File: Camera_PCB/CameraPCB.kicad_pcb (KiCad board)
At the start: 6 copper layers, 51 parts, among them J2 USB_A, U1 V3s-eLQFP128, Y2 Crystal_GND3, Y4 Crystal_GND24

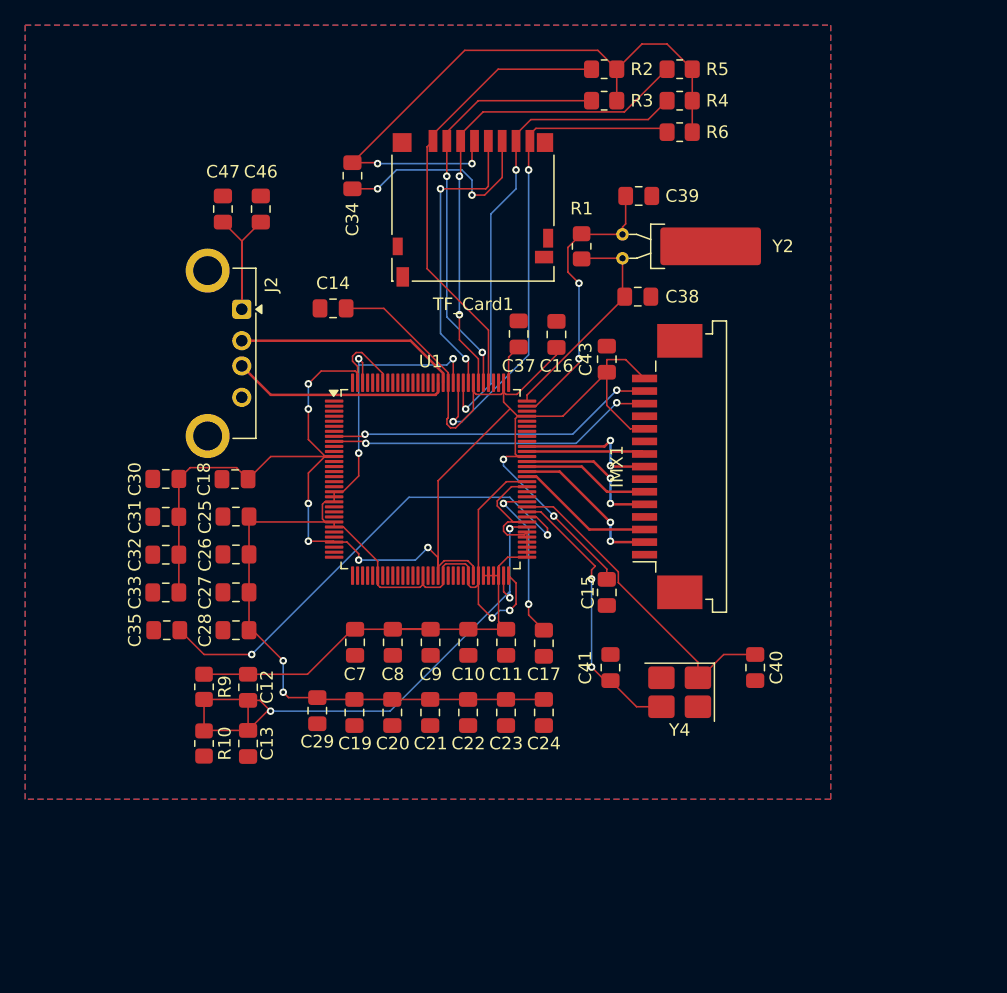
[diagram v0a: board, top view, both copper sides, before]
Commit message: Schematic done, thoroughly reviewed by Jack, should get reviewed by Connor if possible.
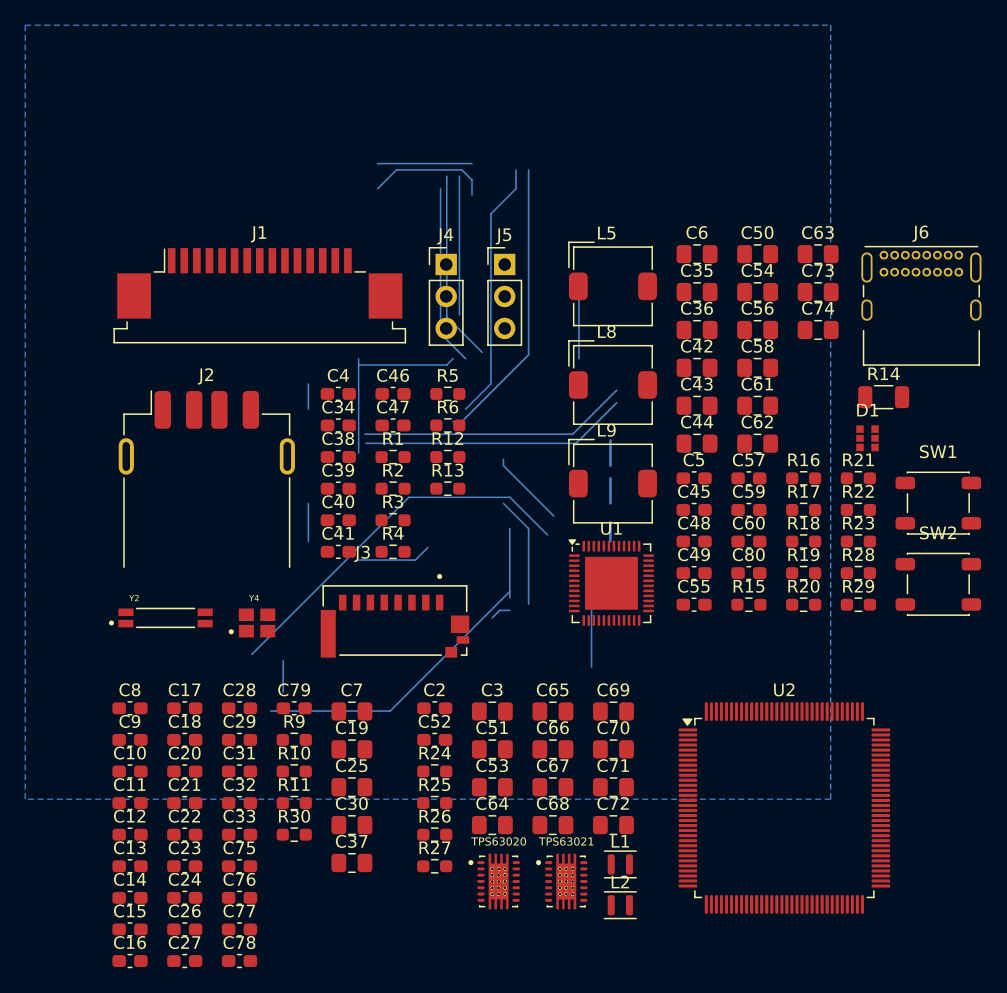
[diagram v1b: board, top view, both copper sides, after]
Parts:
- removed IMX1: ~, Connector_FFC-FPC:TE_1-84952-5_1x15-1MP_P1.0mm_Horizontal
- removed TF_Card1: ~, Connector_Card:microSD_HC_Hirose_DM3D-SF
- added C2: 0.1u, Capacitor_SMD:C_0603_1608Metric_Pad1.08x0.95mm_HandSolder, F.Cu at (148.0, 125.3)
- added C3: 22u, Capacitor_SMD:C_0805_2012Metric_Pad1.18x1.45mm_HandSolder, F.Cu at (152.6, 125.5)
- added C36: 10u, Capacitor_SMD:C_0805_2012Metric_Pad1.18x1.45mm_HandSolder, F.Cu at (168.9, 95.2)
- added C4: 1u, Capacitor_SMD:C_0603_1608Metric_Pad1.08x0.95mm_HandSolder, F.Cu at (140.4, 100.3)
- added C42: 10u, Capacitor_SMD:C_0805_2012Metric_Pad1.18x1.45mm_HandSolder, F.Cu at (168.9, 98.2)
- added C44: 4.7u, Capacitor_SMD:C_0805_2012Metric_Pad1.18x1.45mm_HandSolder, F.Cu at (168.9, 104.2)
- added C45: 0.1u, Capacitor_SMD:C_0603_1608Metric_Pad1.08x0.95mm_HandSolder, F.Cu at (168.7, 109.5)
- added C48: 1u, Capacitor_SMD:C_0603_1608Metric_Pad1.08x0.95mm_HandSolder, F.Cu at (168.7, 112.0)
- added C49: 1u, Capacitor_SMD:C_0603_1608Metric_Pad1.08x0.95mm_HandSolder, F.Cu at (168.7, 114.5)
- added C5: 1u, Capacitor_SMD:C_0603_1608Metric_Pad1.08x0.95mm_HandSolder, F.Cu at (168.7, 107.0)
- added C50: 10u, Capacitor_SMD:C_0805_2012Metric_Pad1.18x1.45mm_HandSolder, F.Cu at (173.7, 89.2)
- added C51: 22u, Capacitor_SMD:C_0805_2012Metric_Pad1.18x1.45mm_HandSolder, F.Cu at (152.6, 128.5)
- added C52: 0.1u, Capacitor_SMD:C_0603_1608Metric_Pad1.08x0.95mm_HandSolder, F.Cu at (148.0, 127.8)
- added C53: 10u, Capacitor_SMD:C_0805_2012Metric_Pad1.18x1.45mm_HandSolder, F.Cu at (152.6, 131.5)
- added C54: 10u, Capacitor_SMD:C_0805_2012Metric_Pad1.18x1.45mm_HandSolder, F.Cu at (173.7, 92.2)
- added C55: 1n, Capacitor_SMD:C_0603_1608Metric_Pad1.08x0.95mm_HandSolder, F.Cu at (168.7, 117.0)
- added C56: 10u, Capacitor_SMD:C_0805_2012Metric_Pad1.18x1.45mm_HandSolder, F.Cu at (173.7, 95.2)
- added C57: 1n, Capacitor_SMD:C_0603_1608Metric_Pad1.08x0.95mm_HandSolder, F.Cu at (173.0, 107.0)
- added C58: 10u, Capacitor_SMD:C_0805_2012Metric_Pad1.18x1.45mm_HandSolder, F.Cu at (173.7, 98.2)
- added C59: 0.1u, Capacitor_SMD:C_0603_1608Metric_Pad1.08x0.95mm_HandSolder, F.Cu at (173.0, 109.5)
- added C6: 10u, Capacitor_SMD:C_0805_2012Metric_Pad1.18x1.45mm_HandSolder, F.Cu at (168.9, 89.2)
- added C60: 0.1u, Capacitor_SMD:C_0603_1608Metric_Pad1.08x0.95mm_HandSolder, F.Cu at (173.0, 112.0)
- added C61: 4.7u, Capacitor_SMD:C_0805_2012Metric_Pad1.18x1.45mm_HandSolder, F.Cu at (173.7, 101.2)
- added C62: 10u, Capacitor_SMD:C_0805_2012Metric_Pad1.18x1.45mm_HandSolder, F.Cu at (173.7, 104.2)
- added C63: 10u, Capacitor_SMD:C_0805_2012Metric_Pad1.18x1.45mm_HandSolder, F.Cu at (178.5, 89.2)
- added C64: 10u, Capacitor_SMD:C_0805_2012Metric_Pad1.18x1.45mm_HandSolder, F.Cu at (152.6, 134.6)
- added C65: 10u, Capacitor_SMD:C_0805_2012Metric_Pad1.18x1.45mm_HandSolder, F.Cu at (157.4, 125.5)
- added C66: 10u, Capacitor_SMD:C_0805_2012Metric_Pad1.18x1.45mm_HandSolder, F.Cu at (157.4, 128.5)
- added C67: 10u, Capacitor_SMD:C_0805_2012Metric_Pad1.18x1.45mm_HandSolder, F.Cu at (157.4, 131.5)
- added C68: 10u, Capacitor_SMD:C_0805_2012Metric_Pad1.18x1.45mm_HandSolder, F.Cu at (157.4, 134.6)
- added C69: 10u, Capacitor_SMD:C_0805_2012Metric_Pad1.18x1.45mm_HandSolder, F.Cu at (162.2, 125.5)
- added C70: 10u, Capacitor_SMD:C_0805_2012Metric_Pad1.18x1.45mm_HandSolder, F.Cu at (162.2, 128.5)
- added C71: 10u, Capacitor_SMD:C_0805_2012Metric_Pad1.18x1.45mm_HandSolder, F.Cu at (162.2, 131.5)
- added C72: 10u, Capacitor_SMD:C_0805_2012Metric_Pad1.18x1.45mm_HandSolder, F.Cu at (162.2, 134.6)
- added C73: 4.7u, Capacitor_SMD:C_0805_2012Metric_Pad1.18x1.45mm_HandSolder, F.Cu at (178.5, 92.2)
- added C74: 4.7u, Capacitor_SMD:C_0805_2012Metric_Pad1.18x1.45mm_HandSolder, F.Cu at (178.5, 95.2)
- added C75: 0.1u, Capacitor_SMD:C_0603_1608Metric_Pad1.08x0.95mm_HandSolder, F.Cu at (132.5, 137.8)
- added C76: 0.1u, Capacitor_SMD:C_0603_1608Metric_Pad1.08x0.95mm_HandSolder, F.Cu at (132.5, 140.3)
- added C77: 0.1u, Capacitor_SMD:C_0603_1608Metric_Pad1.08x0.95mm_HandSolder, F.Cu at (132.5, 142.8)
- added C78: 0.1u, Capacitor_SMD:C_0603_1608Metric_Pad1.08x0.95mm_HandSolder, F.Cu at (132.5, 145.4)
- added C79: 0.1u, Capacitor_SMD:C_0603_1608Metric_Pad1.08x0.95mm_HandSolder, F.Cu at (136.9, 125.3)
- added C80: 1u, Capacitor_SMD:C_0603_1608Metric_Pad1.08x0.95mm_HandSolder, F.Cu at (173.0, 114.5)
- added D1: LED_RGB, BackupCamCustomParts:RGB_LED IN-S66TFT5R5G5B, F.Cu at (182.4, 103.8)
- added J1: MIPI-CSI2, Connector_FFC-FPC:TE_1-84952-5_1x15-1MP_P1.0mm_Horizontal, F.Cu at (134.1, 91.5)
- added J3: SDA, BackupCamCustomParts:AMPHENOL_10067099-200LF, F.Cu at (144.9, 118.3)
- added J4: UART_0, Connector_PinHeader_2.54mm:PinHeader_1x03_P2.54mm_Vertical, F.Cu at (148.9, 90.0)
- added J5: UART_2, Connector_PinHeader_2.54mm:PinHeader_1x03_P2.54mm_Vertical, F.Cu at (153.6, 90.0)
- added J6: USB_C_Receptacle_PowerOnly_6P, Connector_USB:USB_C_Receptacle_GCT_USB4085, F.Cu at (183.7, 89.3)
- added L1: 1uH, Inductor_SMD:L_Murata_DFE201610P, F.Cu at (162.8, 137.7)
- added L2: 1uH, Inductor_SMD:L_Murata_DFE201610P, F.Cu at (162.8, 140.9)
- added L5: 4.7uH, Inductor_SMD:L_TDK_SLF6045, F.Cu at (162.2, 91.8)
- added L8: 4.7uH, Inductor_SMD:L_TDK_SLF6045, F.Cu at (162.2, 99.6)
- added L9: 4.7uH, Inductor_SMD:L_TDK_SLF6045, F.Cu at (162.2, 107.4)
- added R11: 240, Resistor_SMD:R_0603_1608Metric_Pad0.98x0.95mm_HandSolder, F.Cu at (136.9, 132.8)
- added R12: 4.7k, Resistor_SMD:R_0603_1608Metric_Pad0.98x0.95mm_HandSolder, F.Cu at (149.1, 105.3)
- added R13: 4.7k, Resistor_SMD:R_0603_1608Metric_Pad0.98x0.95mm_HandSolder, F.Cu at (149.1, 107.8)
- added R14: 0.03, Resistor_SMD:R_1206_3216Metric, F.Cu at (183.7, 100.6)
- added R15: 200k, Resistor_SMD:R_0603_1608Metric_Pad0.98x0.95mm_HandSolder, F.Cu at (173.0, 117.0)
- added R16: 5.1k, Resistor_SMD:R_0603_1608Metric_Pad0.98x0.95mm_HandSolder, F.Cu at (177.3, 107.0)
- added R17: 5.1k, Resistor_SMD:R_0603_1608Metric_Pad0.98x0.95mm_HandSolder, F.Cu at (177.3, 109.5)
- added R18: 47k, Resistor_SMD:R_0603_1608Metric_Pad0.98x0.95mm_HandSolder, F.Cu at (177.3, 112.0)
- added R19: 470, Resistor_SMD:R_0603_1608Metric_Pad0.98x0.95mm_HandSolder, F.Cu at (177.3, 114.5)
- added R20: 1k, Resistor_SMD:R_0603_1608Metric_Pad0.98x0.95mm_HandSolder, F.Cu at (177.3, 117.0)
- added R21: 1k, Resistor_SMD:R_0603_1608Metric_Pad0.98x0.95mm_HandSolder, F.Cu at (181.7, 107.0)
- added R22: 0, Resistor_SMD:R_0603_1608Metric_Pad0.98x0.95mm_HandSolder, F.Cu at (181.7, 109.5)
- added R23: 0, Resistor_SMD:R_0603_1608Metric_Pad0.98x0.95mm_HandSolder, F.Cu at (181.7, 112.0)
- added R24: 1.62M, Resistor_SMD:R_0603_1608Metric_Pad0.98x0.95mm_HandSolder, F.Cu at (148.0, 130.3)
- added R25: 180k, Resistor_SMD:R_0603_1608Metric_Pad0.98x0.95mm_HandSolder, F.Cu at (148.0, 132.8)
- added R26: 768k, Resistor_SMD:R_0603_1608Metric_Pad0.98x0.95mm_HandSolder, F.Cu at (148.0, 135.3)
- added R27: 137k, Resistor_SMD:R_0603_1608Metric_Pad0.98x0.95mm_HandSolder, F.Cu at (148.0, 137.8)
- added R28: 470, Resistor_SMD:R_0603_1608Metric_Pad0.98x0.95mm_HandSolder, F.Cu at (181.7, 114.5)
- added R29: 470, Resistor_SMD:R_0603_1608Metric_Pad0.98x0.95mm_HandSolder, F.Cu at (181.7, 117.0)
- added R30: 200k 1%, Resistor_SMD:R_0603_1608Metric_Pad0.98x0.95mm_HandSolder, F.Cu at (136.9, 135.3)
- added SW1: PWR, Button_Switch_SMD:SW_SPST_PTS647_Sx38, F.Cu at (188.1, 109.0)
- added SW2: RST, Button_Switch_SMD:SW_SPST_PTS647_Sx38, F.Cu at (188.1, 115.4)
- added TPS63020: ~, BackupCamCustomParts:IC_TPS63020DSJT, F.Cu at (153.1, 139.0)
- added TPS63021: ~, BackupCamCustomParts:IC_TPS63020DSJT, F.Cu at (158.5, 139.0)
- added U2: V3s-eLQFP128, Package_QFP:LQFP-128_14x14mm_P0.4mm, F.Cu at (175.8, 133.2)
- C10: value 104 -> 1u; footprint Capacitor_SMD:C_0805_2012Metric_Pad1.18x1.45mm_HandSolder -> Capacitor_SMD:C_0603_1608Metric_Pad1.08x0.95mm_HandSolder
- C11, C12, C13, C14, C15, C16, C17, C18, C22, C23, C24, C28, C29, C32, C33, C34, C46: value 104 -> 0.1u; footprint Capacitor_SMD:C_0805_2012Metric_Pad1.18x1.45mm_HandSolder -> Capacitor_SMD:C_0603_1608Metric_Pad1.08x0.95mm_HandSolder
- C19, C25, C30, C7: value 10uF -> 10u
- C20, C21, C26, C27, C31, C47, C8, C9: value 1uF -> 1u; footprint Capacitor_SMD:C_0805_2012Metric_Pad1.18x1.45mm_HandSolder -> Capacitor_SMD:C_0603_1608Metric_Pad1.08x0.95mm_HandSolder
- C35: value 240 -> 10u
- C37: value 4.7uF -> 4.7u
- C38, C39, C40, C41: value 18pF -> 18p; footprint Capacitor_SMD:C_0805_2012Metric_Pad1.18x1.45mm_HandSolder -> Capacitor_SMD:C_0603_1608Metric_Pad1.08x0.95mm_HandSolder
- C43: value 1uF -> 10u
- J2: footprint Connector_USB:USB_A_Connfly_DS1095 -> Connector_USB:USB_A_Receptacle_GCT_USB1046
- R1, R10, R2, R3, R4, R5, R6, R9: footprint Resistor_SMD:R_0805_2012Metric_Pad1.20x1.40mm_HandSolder -> Resistor_SMD:R_0603_1608Metric_Pad0.98x0.95mm_HandSolder
- U1: value V3s-eLQFP128 -> AXP203; footprint Package_QFP:LQFP-128_14x14mm_P0.4mm -> Package_DFN_QFN:QFN-48-1EP_6x6mm_P0.4mm_EP4.2x4.2mm
- Y2: value Crystal_GND3 -> 32.768kHz XTAL; footprint Crystal:Crystal_C38-LF_D3.0mm_L8.0mm_Horizontal_1EP_style1 -> BackupCamCustomParts:XTAL_ECS-.327-12.5-38-TR
- Y4: value Crystal_GND24 -> 24MHz XTAL; footprint Crystal:Crystal_SMD_3225-4Pin_3.2x2.5mm_HandSoldering -> BackupCamCustomParts:XTAL_ECS-240-12-36-AGN-TR
- moved C16 60.2 mm to (123.8, 145.4), turned to 0 degrees
- moved C35 50.0 mm to (168.9, 92.2)
- moved C14 49.5 mm to (123.8, 140.3)
- moved C15 46.4 mm to (123.8, 142.8), turned to 0 degrees
- moved Y2 46.2 mm to (126.7, 118.1), turned to 0 degrees
- moved C37 44.1 mm to (141.5, 137.6), turned to 0 degrees
- moved R4 42.5 mm to (144.7, 112.8), turned to 0 degrees
- moved R3 37.3 mm to (144.7, 110.3), turned to 0 degrees
- moved R2 37.3 mm to (144.7, 107.8), turned to 0 degrees
- moved C40 35.1 mm to (140.4, 110.3), turned to 0 degrees
- moved Y4 34.0 mm to (133.9, 118.5), turned to 0 degrees
- moved C39 33.3 mm to (140.4, 107.8)
- moved C11 32.5 mm to (123.8, 132.8), turned to 0 degrees
- moved C24 32.1 mm to (128.2, 140.3), turned to 0 degrees
- moved R5 31.7 mm to (149.1, 100.3), turned to 0 degrees
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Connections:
- C10 pad 1: GNDREF -> GND
- C11 pad 1: GNDREF -> GND
- C13 pad 1: GNDREF -> GND
- C14 pad 1: GNDREF -> GND
- C15 pad 1: GNDREF -> GND
- C16 pad 1: GNDREF -> GND
- C16 pad 2: HPVCC -> VCC-RTC
- C17 pad 1: GNDREF -> GND
- C17 pad 2: VCC-PLL -> AVCC
- C18 pad 1: GNDREF -> GND
- C19 pad 1: GNDREF -> GND
- C20 pad 1: GNDREF -> GND
- C21 pad 1: GNDREF -> GND
- C22 pad 1: GNDREF -> GND
- C23 pad 1: GNDREF -> GND
- C24 pad 1: GNDREF -> GND
- C25 pad 1: GNDREF -> GND
- C26 pad 1: GNDREF -> GND
- C27 pad 1: GNDREF -> GND
- C28 pad 1: GNDREF -> GND
- C29 pad 1: GNDREF -> GND
- C30 pad 1: GNDREF -> GND
- C31 pad 1: GNDREF -> GND
- C32 pad 1: GNDREF -> GND
- C33 pad 1: GNDREF -> GND
- C34 pad 1: VDD -> HPVCC
- C34 pad 2: GNDREF -> GND
- C35 pad 1: GNDREF -> VBAT
- C35 pad 2: SZQ -> GND
- C37 pad 1: GNDREF -> GND
- C38 pad 2: GNDREF -> GND
- C39 pad 2: GNDREF -> GND
- C40 pad 2: GNDREF -> GND
- C41 pad 1: GNDREF -> GND
- C43 pad 1: HPVCC -> GND
- C43 pad 2: GNDREF -> VIPS
- C46 pad 1: GNDREF -> +5V
- C46 pad 2: +5V -> GND
- C47 pad 1: GNDREF -> +5V
- C47 pad 2: +5V -> GND
- C7 pad 1: GNDREF -> GND
- C8 pad 1: GNDREF -> GND
- C9 pad 1: GNDREF -> GND
- J2 pad 4: GNDREF -> GND
- J2 pad 5: GNDREF -> GND
- R10 pad 2: GNDREF -> GND
- R2 pad 1: VDD -> HPVCC
- R3 pad 1: VDD -> HPVCC
- R4 pad 1: VDD -> HPVCC
- R5 pad 1: VDD -> HPVCC
- R6 pad 1: VDD -> HPVCC
- U1 pad 1: unconnected-(U1-PG4-Pad1) -> TWI0_SDA
- U1 pad 10: unconnected-(U1-PE20-Pad10) -> VDD-CPU
- U1 pad 11: unconnected-(U1-PE19-Pad11) -> Net-(U1-LD04)
- U1 pad 12: HPVCC -> AVCC
- U1 pad 13: unconnected-(U1-PE18-Pad13) -> +3V3
- U1 pad 14: unconnected-(U1-PE17-Pad14) -> VIPS
- U1 pad 15: unconnected-(U1-PE16-Pad15) -> Net-(U1-LX3)
- U1 pad 16: unconnected-(U1-PE15-Pad16) -> GND
- U1 pad 17: unconnected-(U1-PE14-Pad17) -> VCC-DRAM
- U1 pad 19: VDD-CPU -> unconnected-(U1-GPIO0-Pad19)
- U1 pad 2: unconnected-(U1-PG3-Pad2) -> TWI0_SCK
- U1 pad 20: VDD-CPU -> PWREN
- U1 pad 21: VDD-CPU -> VIPS
- U1 pad 22: unconnected-(U1-PE12-Pad22) -> GNDA
- U1 pad 23: unconnected-(U1-PE11-Pad23) -> Net-(U1-BIAS)
- U1 pad 24: unconnected-(U1-PE10-Pad24) -> Net-(U1-VREF)
- U1 pad 25: VDD-CPU -> PGOOD
- U1 pad 26: VDD-CPU -> VINT
- U1 pad 27: unconnected-(U1-PE9-Pad27) -> VINT
- U1 pad 28: unconnected-(U1-PE8-Pad28) -> VCC-RTC
- U1 pad 29: HPVCC -> GND
- U1 pad 32: unconnected-(U1-PE5-Pad32) -> VBUS
- U1 pad 33: unconnected-(U1-PE4-Pad33) -> VBUS
- U1 pad 34: unconnected-(U1-PE3-Pad34) -> VIPS
- U1 pad 35: unconnected-(U1-PE2-Pad35) -> VIPS
- U1 pad 36: unconnected-(U1-PE1-Pad36) -> CHGLED
- U1 pad 38: VDD-CPU -> VBAT
- U1 pad 39: unconnected-(U1-PB0-Pad39) -> VBAT
- U1 pad 4: unconnected-(U1-PG1-Pad4) -> Net-(U1-N_OE)
- U1 pad 41: unconnected-(U1-PB2-Pad41) -> Net-(U1-LDO3)
- U1 pad 42: unconnected-(U1-PB3-Pad42) -> VBAT
- U1 pad 43: unconnected-(U1-PB4-Pad43) -> Net-(U1-CHSENSE)
- U1 pad 44: unconnected-(U1-PB5-Pad44) -> VIPS
- U1 pad 45: unconnected-(U1-PB6-Pad45) -> Net-(U1-LX1)
- U1 pad 46: unconnected-(U1-PB7-Pad46) -> GND
- U1 pad 47: VDD-CPU -> Net-(U1-PWRON)
- U1 pad 48: unconnected-(U1-PB8-Pad48) -> IRQ
- U1 pad 49: unconnected-(U1-PB9-Pad49) -> GND
- U1 pad 6: unconnected-(U1-PE24-Pad6) -> Net-(U1-N_VBUSEN)
- U1 pad 7: unconnected-(U1-PE23-Pad7) -> VIPS
- U1 pad 8: CSI_SDA -> Net-(U1-LX2)
- U1 pad 9: CSI-SCK -> GND
- Y2 pad 3: GNDREF -> GND
- Y4 pad 2: GNDREF -> GND
- Y4 pad 4: GNDREF -> GND
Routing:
- net HPVCC: track 154.1 -> 17.1 mm, vias 8 -> 0
- net VDD-CPU: track 109.9 -> 19.4 mm, vias 7 -> 0
- net VDD: track 51.9 -> 0.00 mm, vias 2 -> 0
- net VCC-DRAM: track 50.1 -> 0.00 mm
- net SDC0_D2: track 36.7 -> 0.00 mm
- net SDC0_CMD: track 38.9 -> 11.0 mm, vias 2 -> 0
- net CSI-SCK: track 26.1 -> 0.00 mm, vias 2 -> 0
- net (no net): track 0.00 -> 26.0 mm
- net X24MIN: track 25.7 -> 0.00 mm
- net UART2_TX: track 0.00 -> 21.3 mm
- net SVREF: track 48.3 -> 28.4 mm, vias 3 -> 0
- net SDC0_D3: track 33.6 -> 15.2 mm, vias 2 -> 0
- net SDC0_D0: track 38.8 -> 20.7 mm, vias 2 -> 0
- net X32KIN: track 18.0 -> 0.00 mm
- net USB_N: track 17.8 -> 0.00 mm
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- added copper zone on In1.Cu, net (none)
- added copper zone on In2.Cu, net (none)
- removed copper zone on F.Cu, net GNDREF
- removed copper zone on In2.Cu, net VCC-PLL
- removed copper zone on In1.Cu, net VDD

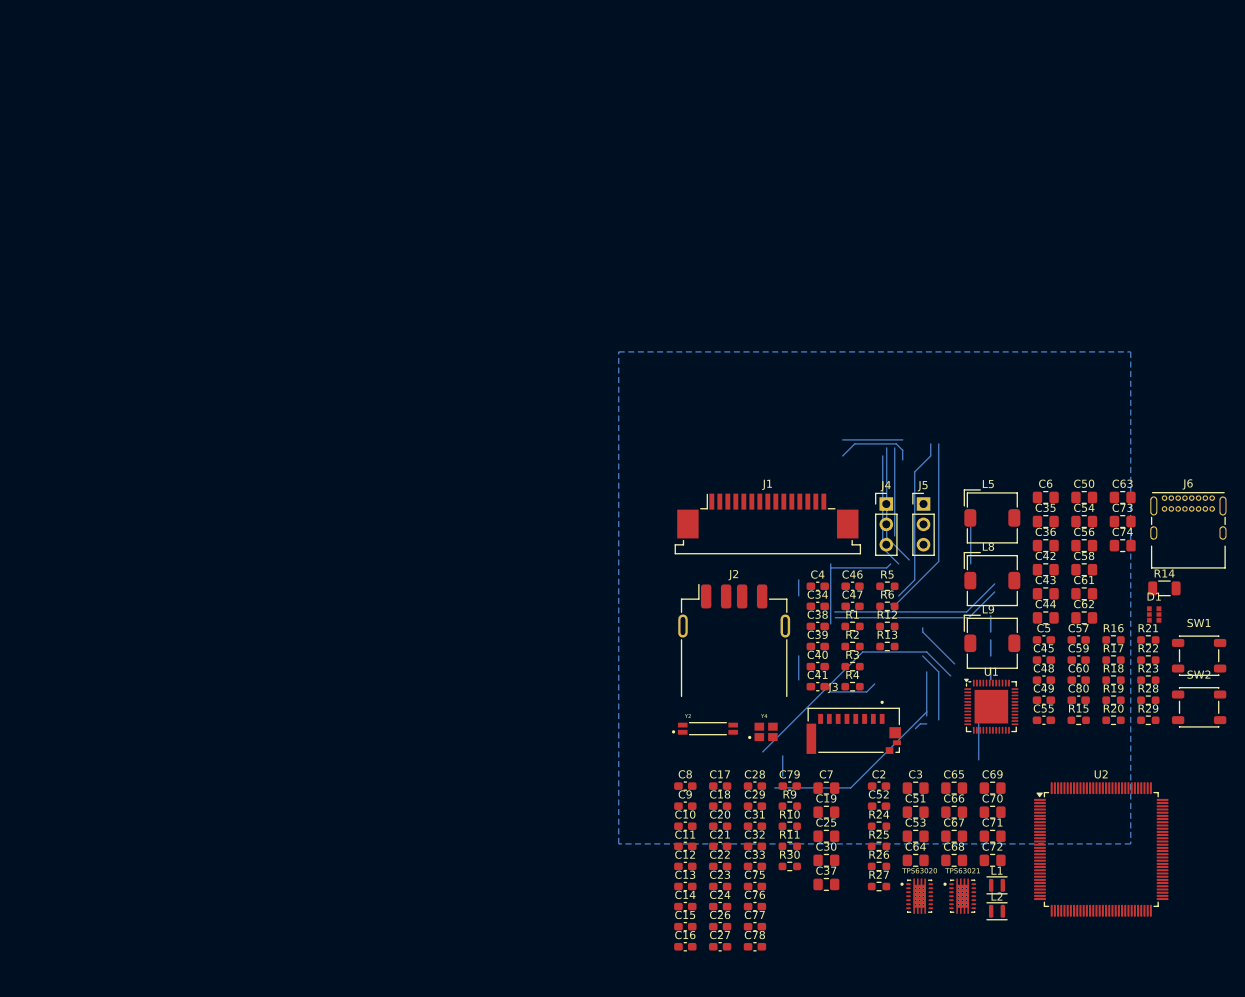
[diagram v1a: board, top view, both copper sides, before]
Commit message: Thorough Camera PCB Review by Jack
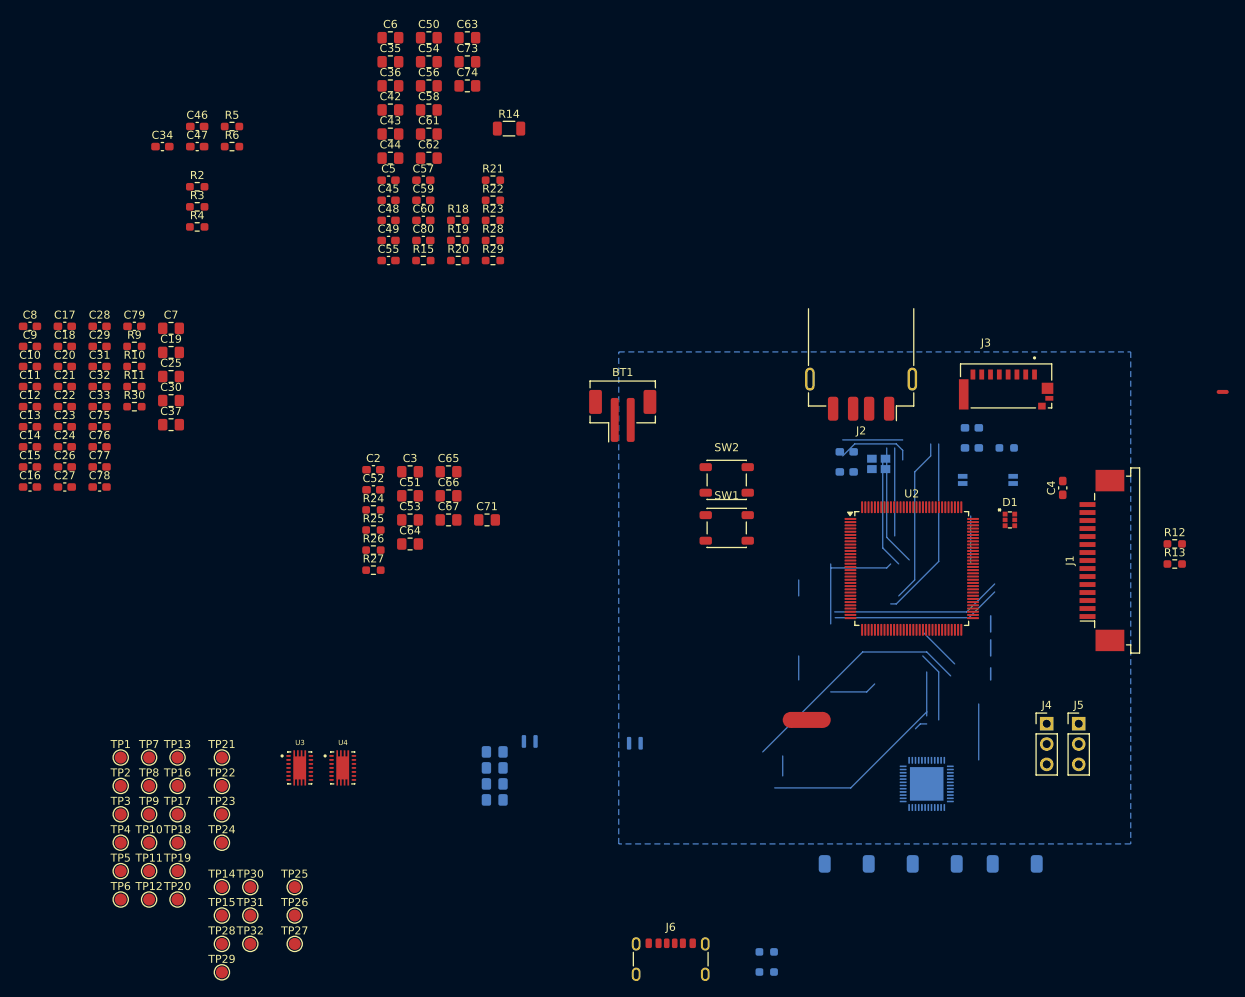
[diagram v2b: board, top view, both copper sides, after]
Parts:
- removed TPS63020, TPS63021: ~, BackupCamCustomParts:IC_TPS63020DSJT
- added BT1: B2B-PH-SM4-TB, Connector_JST:JST_PH_B2B-PH-SM4-TB_1x02-1MP_P2.00mm_Vertical, F.Cu at (116.0, 79.0)
- added NT1: NetTie_2, NetTie:NetTie-2_SMD_Pad2.0mm, F.Cu at (139.0, 117.0)
- added NT2: NetTie_2, NetTie:NetTie-2_SMD_Pad0.5mm, F.Cu at (191.0, 76.0)
- added TP1: VBAT, TestPoint:TestPoint_Pad_D1.5mm, F.Cu at (53.2, 121.7)
- added TP10: RST, TestPoint:TestPoint_Pad_D1.5mm, F.Cu at (56.8, 132.3)
- added TP11: STAT, TestPoint:TestPoint_Pad_D1.5mm, F.Cu at (56.8, 135.9)
- added TP12: PON, TestPoint:TestPoint_Pad_D1.5mm, F.Cu at (56.8, 139.4)
- added TP13: NOE, TestPoint:TestPoint_Pad_D1.5mm, F.Cu at (60.4, 121.7)
- added TP14: SVREF, TestPoint:TestPoint_Pad_D1.5mm, F.Cu at (65.9, 137.9)
- added TP15: SZQ, TestPoint:TestPoint_Pad_D1.5mm, F.Cu at (65.9, 141.4)
- added TP16: 3.0V, TestPoint:TestPoint_Pad_D1.5mm, F.Cu at (60.4, 125.2)
- added TP17: SCK0, TestPoint:TestPoint_Pad_D1.5mm, F.Cu at (60.4, 128.8)
- added TP18: SDA0, TestPoint:TestPoint_Pad_D1.5mm, F.Cu at (60.4, 132.3)
- added TP19: PEN, TestPoint:TestPoint_Pad_D1.5mm, F.Cu at (60.4, 135.9)
- added TP2: VIPS, TestPoint:TestPoint_Pad_D1.5mm, F.Cu at (53.2, 125.2)
- added TP20: CHS, TestPoint:TestPoint_Pad_D1.5mm, F.Cu at (60.4, 139.4)
- added TP21: 5V, TestPoint:TestPoint_Pad_D1.5mm, F.Cu at (65.9, 121.7)
- added TP22: 3V3, TestPoint:TestPoint_Pad_D1.5mm, F.Cu at (65.9, 125.2)
- added TP23: 3V3FB, TestPoint:TestPoint_Pad_D1.5mm, F.Cu at (65.9, 128.8)
- added TP24: 5V0FB, TestPoint:TestPoint_Pad_D1.5mm, F.Cu at (65.9, 132.3)
- added TP25: CSCK, TestPoint:TestPoint_Pad_D1.5mm, F.Cu at (75.0, 137.9)
- added TP26: CSDA, TestPoint:TestPoint_Pad_D1.5mm, F.Cu at (75.0, 141.4)
- added TP27: CEN, TestPoint:TestPoint_Pad_D1.5mm, F.Cu at (75.0, 145.0)
- added TP28: GND, TestPoint:TestPoint_Pad_D1.5mm, F.Cu at (65.9, 145.0)
- added TP29: GND, TestPoint:TestPoint_Pad_D1.5mm, F.Cu at (65.9, 148.6)
- added TP3: 1V2, TestPoint:TestPoint_Pad_D1.5mm, F.Cu at (53.2, 128.8)
- added TP30: GND, TestPoint:TestPoint_Pad_D1.5mm, F.Cu at (69.5, 137.9)
- added TP31: GND, TestPoint:TestPoint_Pad_D1.5mm, F.Cu at (69.5, 141.4)
- added TP32: GND, TestPoint:TestPoint_Pad_D1.5mm, F.Cu at (69.5, 145.0)
- added TP4: 1V8, TestPoint:TestPoint_Pad_D1.5mm, F.Cu at (53.2, 132.3)
- added TP5: VBUS, TestPoint:TestPoint_Pad_D1.5mm, F.Cu at (53.2, 135.9)
- added TP6: VINT, TestPoint:TestPoint_Pad_D1.5mm, F.Cu at (53.2, 139.4)
- added TP7: 3.0V, TestPoint:TestPoint_Pad_D1.5mm, F.Cu at (56.8, 121.7)
- added TP8: VRTC, TestPoint:TestPoint_Pad_D1.5mm, F.Cu at (56.8, 125.2)
- added TP9: PGOOD, TestPoint:TestPoint_Pad_D1.5mm, F.Cu at (56.8, 128.8)
- added U3: TPS63020, BackupCamCustomParts:IC_TPS63020DSJT, F.Cu at (75.6, 123.0)
- added U4: TPS63020, BackupCamCustomParts:IC_TPS63020DSJT, F.Cu at (81.0, 123.0)
- C38, C39, C40, C41, C68, C69, C70, C72, L1, L2, L5, L8, L9, R1, R16, R17, U1, Y2, Y4: moved to B.Cu
- J6: footprint Connector_USB:USB_C_Receptacle_GCT_USB4085 -> Connector_USB:USB_C_Receptacle_GCT_USB4125-xx-x_6P_TopMnt_Horizontal
- R30: value 200k 1% -> 200k
- moved C11 100.1 mm to (41.9, 75.3)
- moved C14 100.1 mm to (41.9, 82.9)
- moved C17 100.1 mm to (46.3, 67.8)
- moved C18 100.1 mm to (46.3, 70.3)
- moved C19 100.1 mm to (59.5, 71.1)
- moved C21 100.1 mm to (46.3, 75.3)
- moved C22 100.1 mm to (46.3, 77.8)
- moved C24 100.1 mm to (46.3, 82.9)
- moved C26 100.1 mm to (46.3, 85.4)
- moved C30 100.1 mm to (59.5, 77.1)
- moved C32 100.1 mm to (50.6, 75.3)
- moved C36 100.1 mm to (87.0, 37.7)
- moved C37 100.1 mm to (59.5, 80.1)
- moved C44 100.1 mm to (87.0, 46.8)
- moved C48 100.1 mm to (86.7, 54.6)
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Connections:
- C2 pad 1: Net-(TPS63020-VINA) -> VIPS
- C4 pad 1: +3V3 -> HPVCC
- C52 pad 1: Net-(TPS63021-VINA) -> VIPS
- C53 pad 1: +3V3 -> HPVCC
- C62 pad 2: +3V3 -> HPVCC
- C64 pad 1: +3V3 -> HPVCC
- C65 pad 1: +3V3 -> HPVCC
- C66 pad 1: +3V3 -> HPVCC
- C66 pad 2: unconnected-(C66-Pad2) -> GND
- C67 pad 1: +3V3 -> HPVCC
- C69 pad 2: unconnected-(C69-Pad2) -> GND
- C80 pad 1: PGOOD -> RESET
- J1 pad 15: +3V3 -> HPVCC
- J1 pad MP: (no net) -> GND
- J3 pad S1: unconnected-(J3-PadS1) -> GND
- J3 pad S2: unconnected-(J3-PadS2) -> GND
- R12 pad 1: +3V3 -> HPVCC
- R13 pad 1: +3V3 -> HPVCC
- R18 pad 2: PGOOD -> RESET
- R20 pad 1: Net-(SW1-K) -> Net-(R20-Pad1)
- R21 pad 1: Net-(SW2-K) -> Net-(R21-Pad1)
- R26 pad 1: +3V3 -> HPVCC
- SW1 pad 1: unconnected-(SW1-Pad1)_1 -> GND
- SW1 pad 2: GND -> Net-(R20-Pad1)
- SW2 pad 1: unconnected-(SW2-Pad1)_1 -> GND
- SW2 pad 2: GND -> Net-(R21-Pad1)
- U1 pad 13: +3V3 -> HPVCC
- U2 pad 9: CSI-SCK -> CSI_SCK
- U2 pad 99: PGOOD -> RESET
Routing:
- net GND: track 2.00 -> 17.8 mm
- net X24MIN: track 0.00 -> 15.2 mm
- net SDC0_D3: track 15.2 -> 0.00 mm
- net (no net): track 26.0 -> 17.1 mm
- net X24MOUT: track 7.00 -> 0.00 mm
- net VDD-CPU: track 19.4 -> 15.2 mm
- net VBUS: track 0.00 -> 2.50 mm
- net SVREF: track 28.4 -> 30.1 mm
